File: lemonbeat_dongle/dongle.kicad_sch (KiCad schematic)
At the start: 10 parts

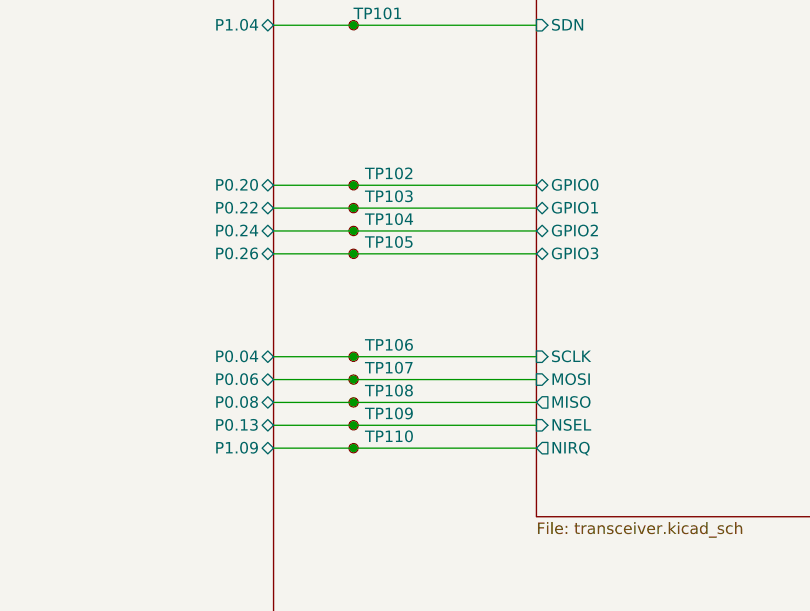
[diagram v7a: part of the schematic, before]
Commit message: dongle: remove GPIO test points; place other test points on PCB
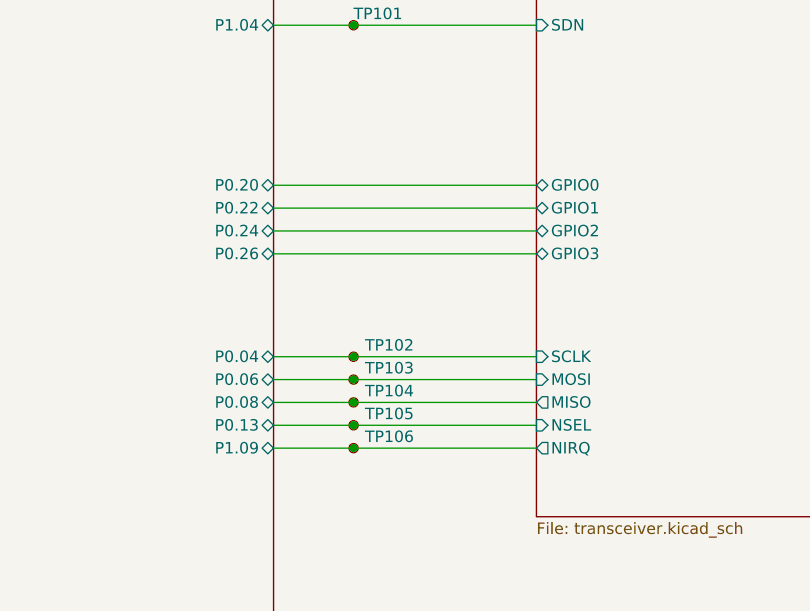
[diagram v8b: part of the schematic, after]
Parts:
- removed TP102, TP103, TP104, TP105: TestPoint_Small, TestPoint:TestPoint_Pad_D1.0mm, symbol Connector:TestPoint_Small
- renumbered TP106 to TP102, TP107 to TP103, TP108 to TP104, TP109 to TP105, TP110 to TP106
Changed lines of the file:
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@@
   (junction (at 125.73 114.3) (diameter 0) (color 0 0 0 0)
   )
-  (junction (at 125.73 97.79) (diameter 0) (color 0 0 0 0)
-  )
-  (junction (at 125.73 95.25) (diameter 0) (color 0 0 0 0)
-  )
-  (junction (at 125.73 90.17) (diameter 0) (color 0 0 0 0)
-  )
   (junction (at 125.73 116.84) (diameter 0) (color 0 0 0 0)
   )
@@
   (junction (at 125.73 109.22) (diameter 0) (color 0 0 0 0)
   )
-  (junction (at 125.73 92.71) (diameter 0) (color 0 0 0 0)
-  )
   (junction (at 125.73 119.38) (diameter 0) (color 0 0 0 0)
   )
-  (wire (pts (xy 116.84 97.79) (xy 125.73 97.79))
-    (stroke (width 0) (type default) (color 0 0 0 0))
-  )
-  (wire (pts (xy 125.73 97.79) (xy 146.05 97.79))
+  (wire (pts (xy 116.84 97.79) (xy 146.05 97.79))
     (stroke (width 0) (type default) (color 0 0 0 0))
   )
@@
     (stroke (width 0) (type default) (color 0 0 0 0))
   )
-  (wire (pts (xy 116.84 95.25) (xy 125.73 95.25))
-    (stroke (width 0) (type default) (color 0 0 0 0))
-  )
   (wire (pts (xy 125.73 116.84) (xy 146.05 116.84))
     (stroke (width 0) (type default) (color 0 0 0 0))
@@
     (stroke (width 0) (type default) (color 0 0 0 0))
   )
-  (wire (pts (xy 125.73 92.71) (xy 146.05 92.71))
-    (stroke (width 0) (type default) (color 0 0 0 0))
-  )
   (wire (pts (xy 116.84 114.3) (xy 125.73 114.3))
     (stroke (width 0) (type default) (color 0 0 0 0))
   )
-  (wire (pts (xy 116.84 92.71) (xy 125.73 92.71))
-    (stroke (width 0) (type default) (color 0 0 0 0))
-  )
-  (wire (pts (xy 116.84 90.17) (xy 125.73 90.17))
-    (stroke (width 0) (type default) (color 0 0 0 0))
-  )
-  (wire (pts (xy 125.73 95.25) (xy 146.05 95.25))
+  (wire (pts (xy 116.84 92.71) (xy 146.05 92.71))
+    (stroke (width 0) (type default) (color 0 0 0 0))
+  )
+  (wire (pts (xy 116.84 90.17) (xy 146.05 90.17))
+    (stroke (width 0) (type default) (color 0 0 0 0))
+  )
+  (wire (pts (xy 116.84 95.25) (xy 146.05 95.25))
     (stroke (width 0) (type default) (color 0 0 0 0))
   )
@@
   )
   (wire (pts (xy 125.73 111.76) (xy 146.05 111.76))
-    (stroke (width 0) (type default) (color 0 0 0 0))
-  )
-  (wire (pts (xy 125.73 90.17) (xy 146.05 90.17))
     (stroke (width 0) (type default) (color 0 0 0 0))
   )
@@
   (symbol (lib_id "Connector:TestPoint_Small") (at 125.73 116.84 0) (unit 1)
     (in_bom yes) (on_board yes)
-    (property "Reference" "TP109" (id 0) (at 127 115.57 0)
+    (property "Reference" "TP105" (id 0) (at 127 115.57 0)
       (effects (font (size 1.27 1.27)) (justify left))
     )
@@
     (pin "1")
   )
-  (symbol (lib_id "Connector:TestPoint_Small") (at 125.73 97.79 0) (unit 1)
-    (in_bom yes) (on_board yes)
-    (property "Reference" "TP105" (id 0) (at 127 96.52 0)
-      (effects (font (size 1.27 1.27)) (justify left))
-    )
-    (property "Value" "TestPoint_Small" (id 1) (at 127 99.0599 0)
-      (effects (font (size 1.27 1.27)) (justify left) hide)
-    )
-    (property "Footprint" "TestPoint:TestPoint_Pad_D1.0mm" (id 2) (at 130.81 97.79 0)
-      (effects (font (size 1.27 1.27)) hide)
-    )
-    (property "Datasheet" "~" (id 3) (at 130.81 97.79 0)
-      (effects (font (size 1.27 1.27)) hide)
-    )
-    (pin "1")
-  )
-  (symbol (lib_id "Connector:TestPoint_Small") (at 125.73 95.25 0) (unit 1)
-    (in_bom yes) (on_board yes)
-    (property "Reference" "TP104" (id 0) (at 127 93.98 0)
-      (effects (font (size 1.27 1.27)) (justify left))
-    )
-    (property "Value" "TestPoint_Small" (id 1) (at 127 96.5199 0)
-      (effects (font (size 1.27 1.27)) (justify left) hide)
-    )
-    (property "Footprint" "TestPoint:TestPoint_Pad_D1.0mm" (id 2) (at 130.81 95.25 0)
-      (effects (font (size 1.27 1.27)) hide)
-    )
-    (property "Datasheet" "~" (id 3) (at 130.81 95.25 0)
-      (effects (font (size 1.27 1.27)) hide)
-    )
-    (pin "1")
-  )
-  (symbol (lib_id "Connector:TestPoint_Small") (at 125.73 92.71 0) (unit 1)
-    (in_bom yes) (on_board yes)
-    (property "Reference" "TP103" (id 0) (at 127 91.44 0)
-      (effects (font (size 1.27 1.27)) (justify left))
-    )
-    (property "Value" "TestPoint_Small" (id 1) (at 127 93.9799 0)
-      (effects (font (size 1.27 1.27)) (justify left) hide)
-    )
-    (property "Footprint" "TestPoint:TestPoint_Pad_D1.0mm" (id 2) (at 130.81 92.71 0)
-      (effects (font (size 1.27 1.27)) hide)
-    )
-    (property "Datasheet" "~" (id 3) (at 130.81 92.71 0)
-      (effects (font (size 1.27 1.27)) hide)
-    )
-    (pin "1")
-  )
   (symbol (lib_id "Connector:TestPoint_Small") (at 125.73 109.22 0) (unit 1)
     (in_bom yes) (on_board yes)
-    (property "Reference" "TP106" (id 0) (at 127 107.95 0)
+    (property "Reference" "TP102" (id 0) (at 127 107.95 0)
       (effects (font (size 1.27 1.27)) (justify left))
     )
@@
   (symbol (lib_id "Connector:TestPoint_Small") (at 125.73 111.76 0) (unit 1)
     (in_bom yes) (on_board yes)
-    (property "Reference" "TP107" (id 0) (at 127 110.49 0)
+    (property "Reference" "TP103" (id 0) (at 127 110.49 0)
       (effects (font (size 1.27 1.27)) (justify left))
     )
@@
   (symbol (lib_id "Connector:TestPoint_Small") (at 125.73 114.3 0) (unit 1)
     (in_bom yes) (on_board yes)
-    (property "Reference" "TP108" (id 0) (at 127 113.03 0)
+    (property "Reference" "TP104" (id 0) (at 127 113.03 0)
       (effects (font (size 1.27 1.27)) (justify left))
     )
@@
     )
     (property "Datasheet" "~" (id 3) (at 130.81 114.3 0)
-      (effects (font (size 1.27 1.27)) hide)
-    )
-    (pin "1")
-  )
-  (symbol (lib_id "Connector:TestPoint_Small") (at 125.73 90.17 0) (unit 1)
-    (in_bom yes) (on_board yes)
-    (property "Reference" "TP102" (id 0) (at 127 88.9 0)
-      (effects (font (size 1.27 1.27)) (justify left))
-    )
-    (property "Value" "TestPoint_Small" (id 1) (at 127 91.4399 0)
-      (effects (font (size 1.27 1.27)) (justify left) hide)
-    )
-    (property "Footprint" "TestPoint:TestPoint_Pad_D1.0mm" (id 2) (at 130.81 90.17 0)
-      (effects (font (size 1.27 1.27)) hide)
-    )
-    (property "Datasheet" "~" (id 3) (at 130.81 90.17 0)
       (effects (font (size 1.27 1.27)) hide)
     )
@@
   (symbol (lib_id "Connector:TestPoint_Small") (at 125.73 119.38 0) (unit 1)
     (in_bom yes) (on_board yes)
-    (property "Reference" "TP110" (id 0) (at 127 118.11 0)
+    (property "Reference" "TP106" (id 0) (at 127 118.11 0)
       (effects (font (size 1.27 1.27)) (justify left))
     )
@@
       (reference "TP101") (unit 1) (value "TestPoint_Small") (footprint "TestPoint:TestPoint_Pad_D1.0mm")
     )
-    (path "/ca8dfa52-27f7-4b39-9e6e-ba1761849c58"
+    (path "/20523571-2c6a-41e9-96fd-ea46bd51a4f1"
       (reference "TP102") (unit 1) (value "TestPoint_Small") (footprint "TestPoint:TestPoint_Pad_D1.0mm")
     )
-    (path "/1dce91db-c33f-4bf8-a742-5fb2e889a15a"
+    (path "/63f66cd6-0409-4099-b8f3-70b266e33f6f"
       (reference "TP103") (unit 1) (value "TestPoint_Small") (footprint "TestPoint:TestPoint_Pad_D1.0mm")
     )
-    (path "/1b560eb6-ca04-4afa-aea9-0c3a3caaa70d"
+    (path "/c5cabc03-a06a-4dfe-a12e-8ede28b8bf94"
       (reference "TP104") (unit 1) (value "TestPoint_Small") (footprint "TestPoint:TestPoint_Pad_D1.0mm")
     )
-    (path "/18a7d445-04bd-4168-93b3-11847e5ec1fe"
+    (path "/064aa6f9-5455-49ca-824e-855a5830f4ed"
       (reference "TP105") (unit 1) (value "TestPoint_Small") (footprint "TestPoint:TestPoint_Pad_D1.0mm")
     )
-    (path "/20523571-2c6a-41e9-96fd-ea46bd51a4f1"
+    (path "/e93b5065-f151-4e71-8530-985c429533a4"
       (reference "TP106") (unit 1) (value "TestPoint_Small") (footprint "TestPoint:TestPoint_Pad_D1.0mm")
     )
-    (path "/63f66cd6-0409-4099-b8f3-70b266e33f6f"
-      (reference "TP107") (unit 1) (value "TestPoint_Small") (footprint "TestPoint:TestPoint_Pad_D1.0mm")
-    )
-    (path "/c5cabc03-a06a-4dfe-a12e-8ede28b8bf94"
-      (reference "TP108") (unit 1) (value "TestPoint_Small") (footprint "TestPoint:TestPoint_Pad_D1.0mm")
-    )
-    (path "/064aa6f9-5455-49ca-824e-855a5830f4ed"
-      (reference "TP109") (unit 1) (value "TestPoint_Small") (footprint "TestPoint:TestPoint_Pad_D1.0mm")
-    )
-    (path "/e93b5065-f151-4e71-8530-985c429533a4"
-      (reference "TP110") (unit 1) (value "TestPoint_Small") (footprint "TestPoint:TestPoint_Pad_D1.0mm")
-    )
     (path "/49f47eff-be71-45a3-baa2-ec3b29bb6923/8929dc0e-0df9-4162-b28e-6dc4f9d8aa2f"
